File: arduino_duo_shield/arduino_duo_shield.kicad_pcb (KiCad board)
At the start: 2 copper layers, 101.6 x 53.3 mm, 46 parts, among them J1 Conn_02x07_Counter_Clockwise, J2 Conn_01x02_Male, J3 Conn_02x03_Counter_Clockwise, J4 Conn_02x03_Counter_Clockwise, J5 Conn_02x03_Counter_Clockwise, J6 Conn_02x03_Counter_Clockwise, K1 G5Q-1, P1 CONN_01X01, P10 Digital, P11 PWM, P12 PWM, P13 Communication, P2 CONN_01X01, P3 CONN_01X01, P4 CONN_01X01, P5 CONN_01X01, P6 CONN_01X01, P7 Power, P8 Analog, P9 Analog, Q1 IRFZ44N, Q2 IRFZ44N, U1 4504, U2 4504, U3 74HC14

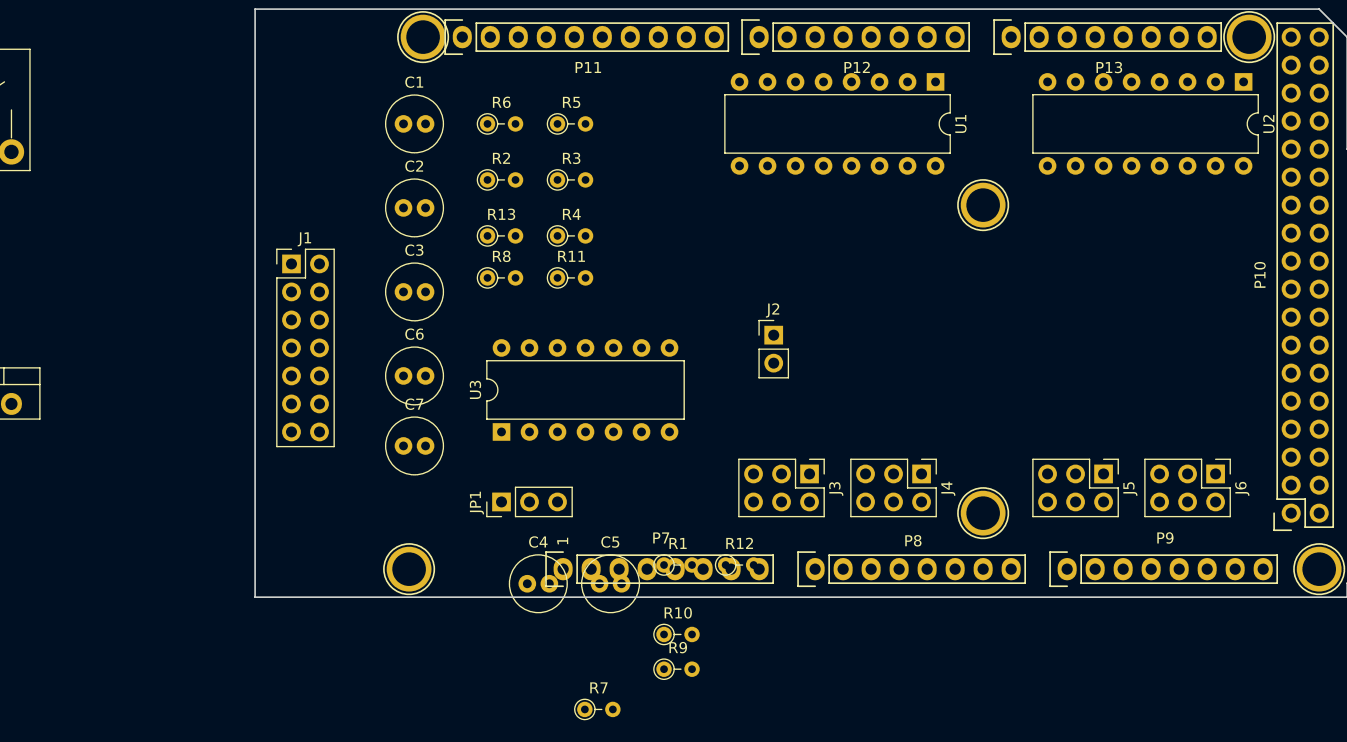
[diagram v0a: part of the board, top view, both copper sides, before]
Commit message: Replace 4x 6x connectors with 1x 24x, add firmware
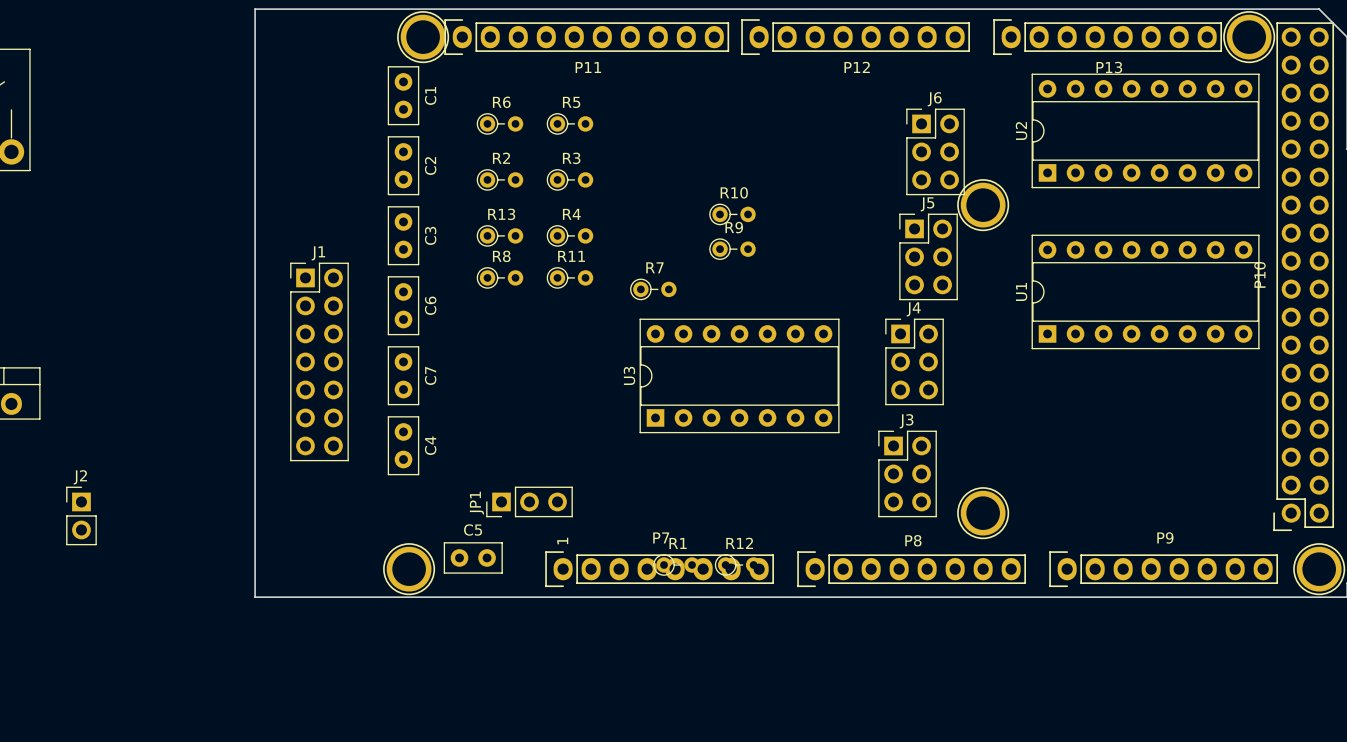
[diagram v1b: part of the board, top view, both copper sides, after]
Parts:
- C1, C2, C3, C4, C5, C6, C7: footprint Capacitor_THT:C_Radial_D5.0mm_H11.0mm_P2.00mm -> Capacitor_THT:C_Disc_D5.0mm_W2.5mm_P2.50mm
- J1: value Conn_02x07_Counter_Clockwise -> Conn_02x07_Odd_Even
- J3, J4, J5, J6: value Conn_02x03_Counter_Clockwise -> Conn_02x03_Odd_Even
- U1, U2: footprint Package_DIP:DIP-16_W7.62mm -> Package_DIP:DIP-16_W7.62mm_Socket
- U3: footprint Package_DIP:DIP-14_W7.62mm -> Package_DIP:DIP-14_W7.62mm_Socket
- moved J2 64.6 mm to (87.6, 113.0)
- moved J6 41.5 mm to (163.8, 78.7), turned to 0 degrees
- moved R10 38.4 mm to (145.6, 87.0)
- moved R7 38.4 mm to (138.4, 93.8)
- moved R9 38.4 mm to (145.6, 90.1)
- moved J5 28.1 mm to (163.2, 88.3), turned to 0 degrees
- moved U1 25.0 mm to (175.3, 97.8), turned to 90 degrees
- moved U2 19.6 mm to (175.3, 83.2), turned to 90 degrees
- moved C4 17.8 mm to (116.8, 106.7), turned to 270 degrees
- moved U3 14.0 mm to (139.7, 105.4)
- moved C5 12.9 mm to (121.9, 118.1)
- moved J4 12.8 mm to (161.9, 97.8), turned to 0 degrees
- moved J3 8.03 mm to (161.3, 108.0), turned to 0 degrees
- moved C7 7.62 mm to (116.8, 100.3), turned to 270 degrees
- moved C6 7.62 mm to (116.8, 94.0), turned to 270 degrees
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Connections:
- J1 pad 11: GND -> /Debounce_x6/SWZmax+
- J1 pad 14: GND -> VREF+
- J1 pad 2: /Debounce_x6/SWXmax+ -> GND
- J1 pad 3: /Debounce_x6/SWYmin+ -> /Debounce_x6/SWXmax+
- J1 pad 4: /Debounce_x6/SWYmax+ -> GND
- J1 pad 5: /Debounce_x6/SWZmin+ -> /Debounce_x6/SWYmin+
- J1 pad 6: /Debounce_x6/SWZmax+ -> GND
- J1 pad 7: GND -> /Debounce_x6/SWYmax+
- J1 pad 8: VREF+ -> GND
- J1 pad 9: GND -> /Debounce_x6/SWZmin+
- J3 pad 2: Net-(J3-Pad2) -> GND
- J3 pad 5: GND -> Net-(J3-Pad5)
- J4 pad 2: Net-(J4-Pad2) -> GND
- J4 pad 5: GND -> Net-(J4-Pad5)
- J5 pad 2: Net-(J5-Pad2) -> GND
- J5 pad 5: GND -> Net-(J5-Pad5)
- J6 pad 2: Net-(J6-Pad2) -> GND
- J6 pad 5: GND -> Net-(J6-Pad5)
- U1 pad 12: Net-(J4-Pad2) -> Net-(J4-Pad3)
- U1 pad 15: Net-(J4-Pad3) -> Net-(J4-Pad5)
- U1 pad 4: Net-(J3-Pad2) -> Net-(J3-Pad3)
- U1 pad 6: Net-(J3-Pad3) -> Net-(J3-Pad5)
- U2 pad 12: Net-(J6-Pad2) -> Net-(J6-Pad3)
- U2 pad 15: Net-(J6-Pad3) -> Net-(J6-Pad5)
- U2 pad 4: Net-(J5-Pad2) -> Net-(J5-Pad3)
- U2 pad 6: Net-(J5-Pad3) -> Net-(J5-Pad5)

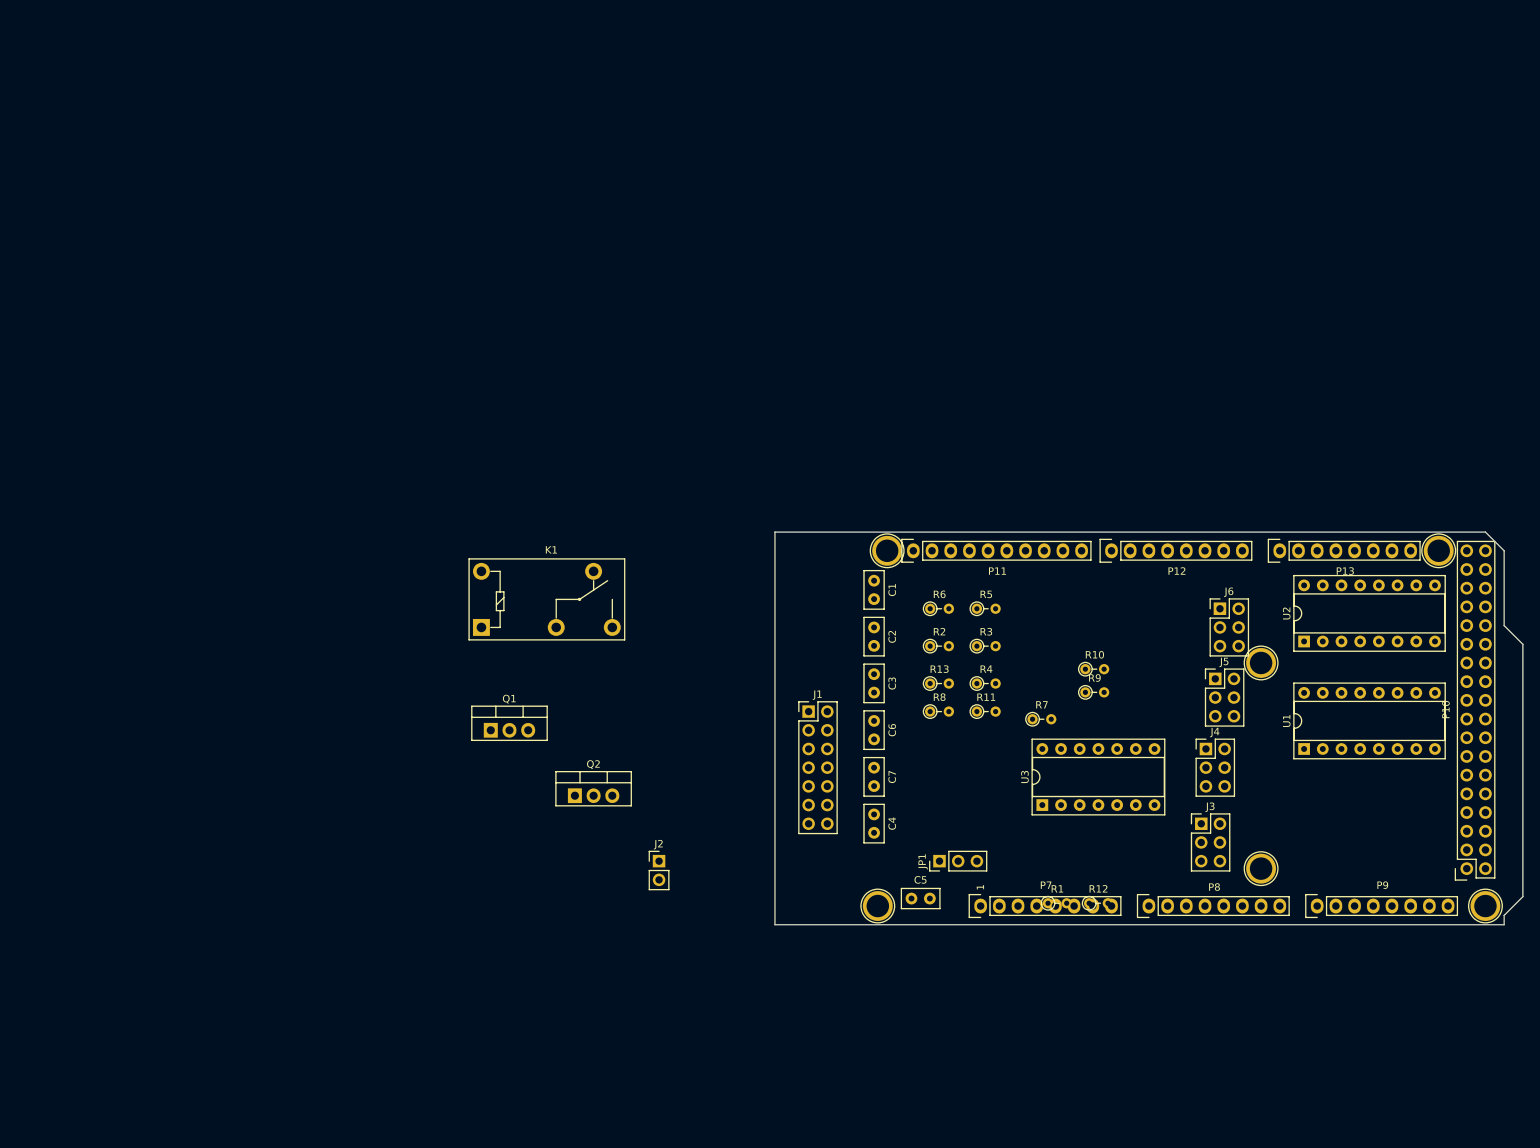
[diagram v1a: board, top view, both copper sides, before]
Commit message: Use only 1 VPOW in spindle control
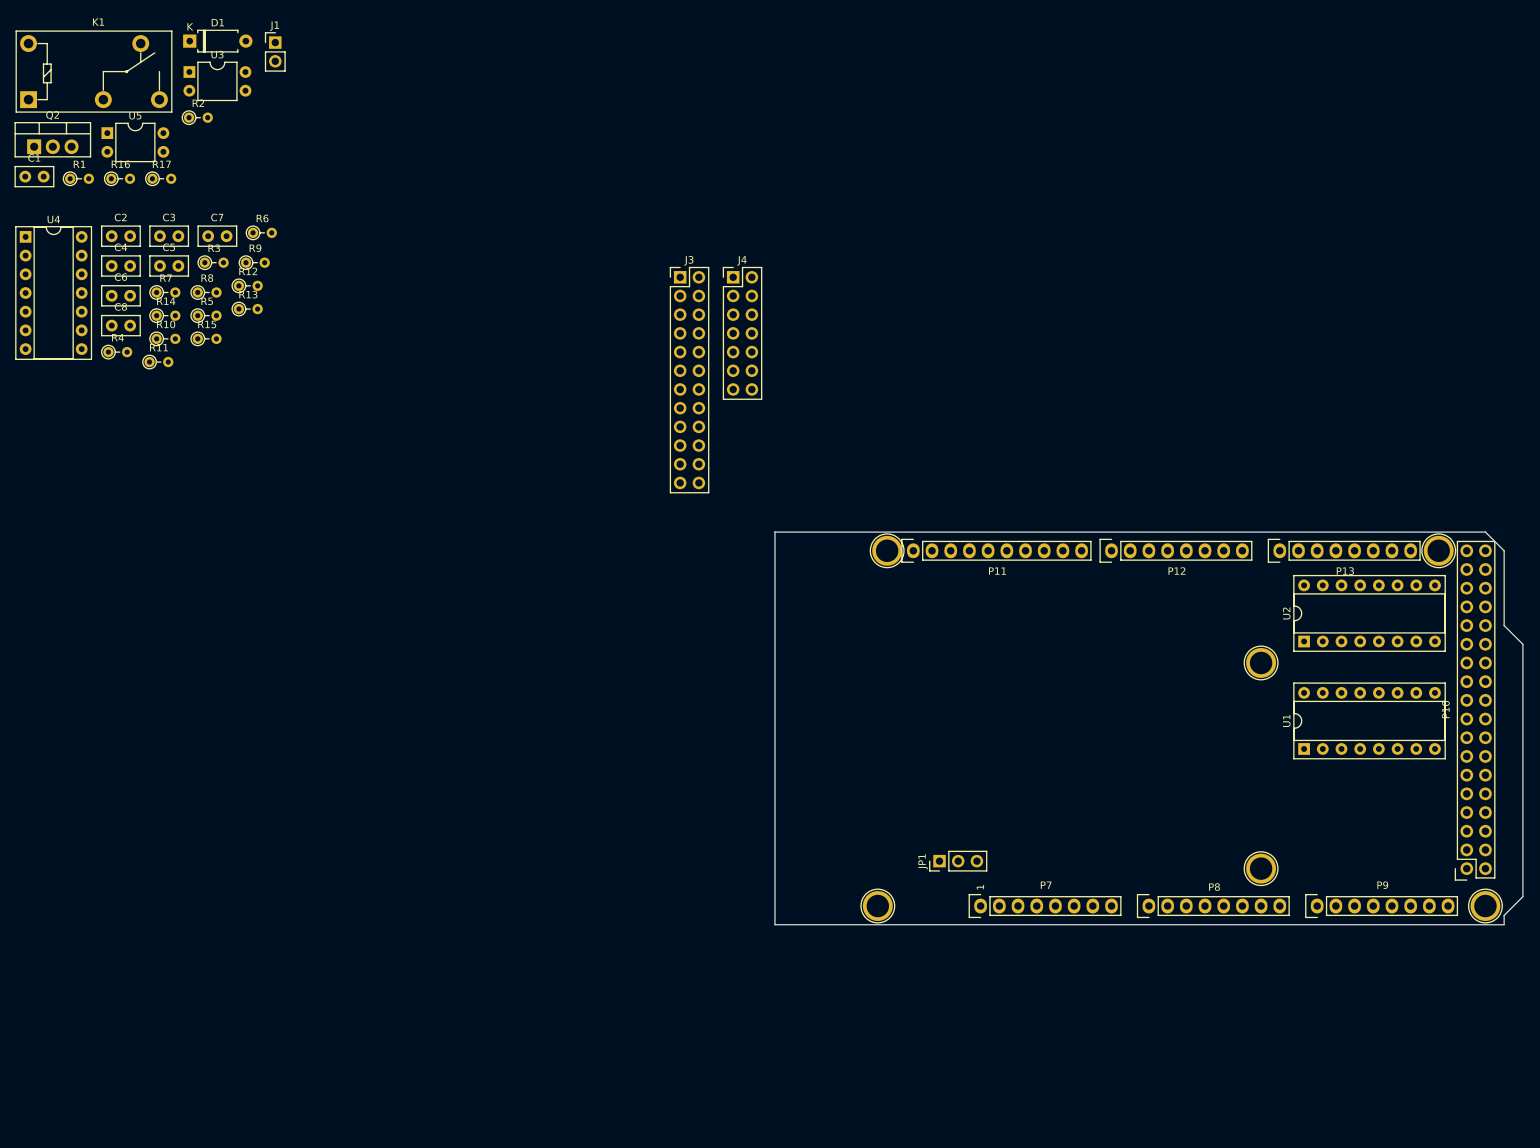
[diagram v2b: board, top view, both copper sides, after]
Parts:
- removed J2: Conn_01x02_Male, Connector_PinHeader_2.54mm:PinHeader_1x02_P2.54mm_Vertical
- removed J5, J6: Conn_02x03_Odd_Even, Connector_PinHeader_2.54mm:PinHeader_2x03_P2.54mm_Vertical
- removed Q1: IRFZ44N, Package_TO_SOT_THT:TO-220-3_Vertical
- added C8: 100p, Capacitor_THT:C_Disc_D5.0mm_W2.5mm_P2.50mm, F.Cu at (13.3, 40.3)
- added D1: DIODE, Diode_THT:D_A-405_P7.62mm_Horizontal, F.Cu at (23.9, 1.63)
- added R14: 10K, Resistor_THT:R_Axial_DIN0204_L3.6mm_D1.6mm_P2.54mm_Vertical, F.Cu at (19.4, 38.9)
- added R15: 10K, Resistor_THT:R_Axial_DIN0204_L3.6mm_D1.6mm_P2.54mm_Vertical, F.Cu at (25.0, 42.1)
- added R16: 1K, Resistor_THT:R_Axial_DIN0204_L3.6mm_D1.6mm_P2.54mm_Vertical, F.Cu at (13.2, 20.3)
- added R17: 220, Resistor_THT:R_Axial_DIN0204_L3.6mm_D1.6mm_P2.54mm_Vertical, F.Cu at (18.8, 20.3)
- added U4: 74HC14, Package_DIP:DIP-14_W7.62mm_Socket, F.Cu at (1.58, 28.2)
- added U5: PC817, Package_DIP:DIP-4_W7.62mm, F.Cu at (12.7, 14.1)
- C1: value 100nF -> 100u
- C2, C3, C4, C5, C6: value 100nF -> 100p
- C7: value 100pF -> 100p
- J1: value Conn_02x07_Odd_Even -> Spindle_Power; footprint Connector_PinHeader_2.54mm:PinHeader_2x07_P2.54mm_Vertical -> Connector_PinHeader_2.54mm:PinHeader_1x02_P2.54mm_Vertical
- J3: value Conn_02x03_Odd_Even -> Motor_Control; footprint Connector_PinHeader_2.54mm:PinHeader_2x03_P2.54mm_Vertical -> Connector_PinHeader_2.54mm:PinHeader_2x12_P2.54mm_Vertical
- J4: value Conn_02x03_Odd_Even -> Limit_Switches; footprint Connector_PinHeader_2.54mm:PinHeader_2x03_P2.54mm_Vertical -> Connector_PinHeader_2.54mm:PinHeader_2x07_P2.54mm_Vertical
- R1: value 10K -> 220
- R2: value 10K -> 1.5K
- U3: value 74HC14 -> PC817; footprint Package_DIP:DIP-14_W7.62mm_Socket -> Package_DIP:DIP-4_W7.62mm
- moved R1 165.3 mm to (7.63, 20.3)
- moved U3 152.8 mm to (23.8, 5.83), turned to 0 degrees
- moved R12 142.7 mm to (30.6, 34.9)
- moved R10 133.9 mm to (19.4, 42.1)
- moved C5 133.4 mm to (19.8, 32.2)
- moved R7 132.4 mm to (19.4, 35.8)
- moved R9 128.1 mm to (31.5, 31.7)
- moved C1 127.7 mm to (1.53, 20.0), turned to 0 degrees
- moved C4 127.6 mm to (13.3, 32.2), turned to 0 degrees
- moved R4 126.3 mm to (12.8, 43.9)
- moved R2 123.7 mm to (23.8, 12.0)
- moved R11 122.0 mm to (18.4, 45.2)
- moved C6 118.6 mm to (13.3, 36.2), turned to 0 degrees
- moved R3 117.1 mm to (25.9, 31.7)
- moved C2 116.4 mm to (13.3, 28.1), turned to 0 degrees
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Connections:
- C1 pad 2: GND -> Net-(C1-Pad2)
- C2 pad 1: Net-(C2-Pad1) -> GND
- C2 pad 2: GND -> Net-(C2-Pad2)
- C3 pad 1: Net-(C3-Pad1) -> GND
- C3 pad 2: GND -> Net-(C3-Pad2)
- C4 pad 1: Net-(C4-Pad1) -> GND
- C4 pad 2: GND -> Net-(C4-Pad2)
- C5 pad 1: Net-(C5-Pad1) -> GND
- C5 pad 2: GND -> Net-(C5-Pad2)
- C6 pad 1: Net-(C6-Pad1) -> GND
- C6 pad 2: GND -> Net-(C6-Pad2)
- C7 pad 1: Probe -> GND
- C7 pad 2: GND -> Net-(C7-Pad2)
- J1 pad 1: /Debounce_x6/SWXmin+ -> Net-(C1-Pad1)
- J1 pad 2: GND -> Net-(C1-Pad2)
- J4 pad 1: Net-(J4-Pad1) -> /sheet5D7EDA0A/SWXmin+
- J4 pad 3: Net-(J4-Pad3) -> /sheet5D7EDA0A/SWXmax+
- J4 pad 5: Net-(J4-Pad5) -> /sheet5D7EDA0A/SWYmin+
- K1 pad 2: Net-(J2-Pad1) -> Net-(C1-Pad1)
- K1 pad 4: PWR -> +24V
- Q2 pad 1: sppwm -> Net-(Q2-Pad1)
- Q2 pad 2: Net-(J2-Pad2) -> Net-(C1-Pad2)
- R1 pad 1: /Debounce_x6/SWXmin+ -> Net-(R1-Pad1)
- R1 pad 2: VREF+ -> sppwm
- R10 pad 1: Net-(C4-Pad1) -> Net-(C5-Pad2)
- R10 pad 2: /Debounce_x6/SWYmax+ -> /sheet5D7EDA0A/SWYmin+
- R11 pad 1: Net-(C5-Pad1) -> /sheet5D7EDA0A/SWXmax+
- R11 pad 2: /Debounce_x6/SWZmin+ -> VREF+
- R12 pad 1: Net-(C6-Pad1) -> Net-(C6-Pad2)
- R12 pad 2: /Debounce_x6/SWZmax+ -> /sheet5D7EDA0A/SWXmax+
- R13 pad 1: Probe -> /sheet5D7EDA0A/SWXmin+
- R2 pad 1: /Debounce_x6/SWXmax+ -> Net-(R2-Pad1)
- R2 pad 2: VREF+ -> Net-(Q2-Pad1)
- R3 pad 1: /Debounce_x6/SWYmin+ -> /sheet5D7EDA0A/SWZmax+
- R4 pad 1: /Debounce_x6/SWYmax+ -> Net-(C2-Pad2)
- R4 pad 2: VREF+ -> /sheet5D7EDA0A/SWZmax+
- R5 pad 1: /Debounce_x6/SWZmin+ -> /sheet5D7EDA0A/SWZmin+
- R6 pad 1: /Debounce_x6/SWZmax+ -> Net-(C3-Pad2)
- R6 pad 2: VREF+ -> /sheet5D7EDA0A/SWZmin+
- R7 pad 1: Net-(C1-Pad1) -> /sheet5D7EDA0A/SWYmax+
- R7 pad 2: /Debounce_x6/SWXmin+ -> VREF+
- R8 pad 1: Net-(C2-Pad1) -> Net-(C4-Pad2)
- R8 pad 2: /Debounce_x6/SWXmax+ -> /sheet5D7EDA0A/SWYmax+
- R9 pad 1: Net-(C3-Pad1) -> /sheet5D7EDA0A/SWYmin+
- R9 pad 2: /Debounce_x6/SWYmin+ -> VREF+
- U1 pad 10: Net-(J4-Pad1) -> Net-(J3-Pad7)
- U1 pad 12: Net-(J4-Pad3) -> Net-(J3-Pad9)
- U1 pad 15: Net-(J4-Pad5) -> Net-(J3-Pad11)
- U2 pad 10: Net-(J6-Pad1) -> Net-(J3-Pad19)
- U2 pad 12: Net-(J6-Pad3) -> Net-(J3-Pad21)
- U2 pad 15: Net-(J6-Pad5) -> Net-(J3-Pad23)
- U2 pad 2: Net-(J5-Pad1) -> Net-(J3-Pad13)
- U2 pad 4: Net-(J5-Pad3) -> Net-(J3-Pad15)
- U2 pad 6: Net-(J5-Pad5) -> Net-(J3-Pad17)
- U3 pad 1: Net-(C1-Pad1) -> Net-(R1-Pad1)
- U3 pad 2: Xmn -> GND
- U3 pad 3: Net-(C2-Pad1) -> Net-(R2-Pad1)
- U3 pad 4: Xmx -> +24V
